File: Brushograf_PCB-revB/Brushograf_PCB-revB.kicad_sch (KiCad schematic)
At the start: 75 parts, among them J1 Conn_01x05_Socket, J12 USB-C PD in, J13 FluidDial pendant, J2 Conn_01x05_Socket, J3 Conn_01x05_Socket, J6 Conn_01x07_Socket, J7 Conn_01x03_Pin, J8 SD_CARD_MICRO_AMPHENOL_114008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, SW1 ESP POWER, U1 ULN2003A, U2 ULN2003A, U3 ULN2003A, U4 ESP32-DevKitC, U6 CH224K, U7 TPS54202, U8 TPS54202

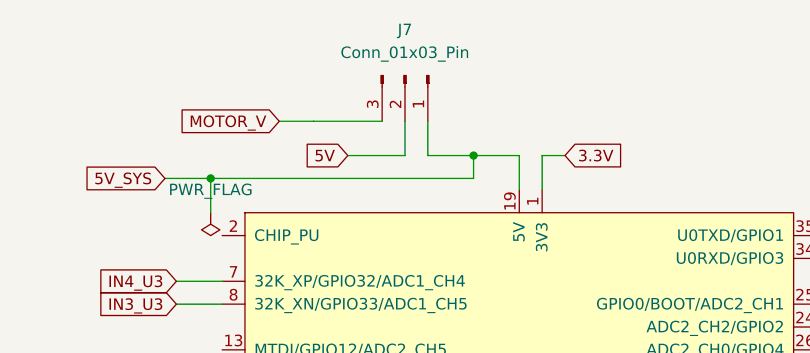
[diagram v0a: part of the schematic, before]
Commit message: Update SW2 to switch, move SW1 for hole clearance, relocate SD card holder to edge
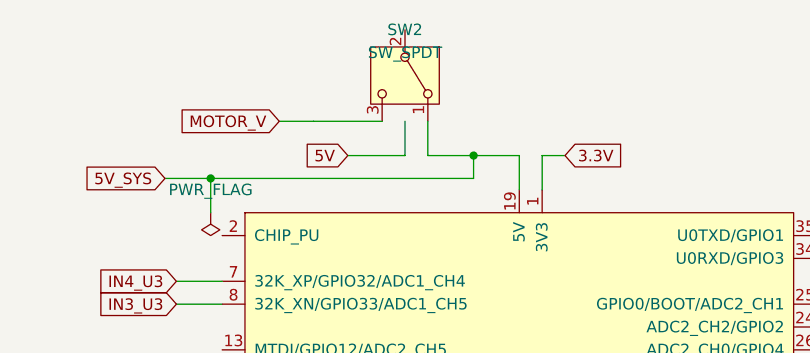
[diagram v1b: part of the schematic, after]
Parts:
- SW2: renamed from J7; value Conn_01x03_Pin -> SW_SPDT; footprint Connector_Molex:Molex_KK-254_AE-6410-03A_1x03_P2.54mm_Vertical -> Button_Switch_THT:SW_Slide_1P2T_EG1218; symbol Connector:Conn_01x03_Pin -> Switch:SW_SPDT
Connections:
- net 5V: no longer SW2.2 (Pin_2)
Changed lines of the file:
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@@
 	)
 	(symbol
-		(lib_id "Connector:Conn_01x03_Pin")
+		(lib_id "Switch:SW_SPDT")
 		(at 177.8 19.05 270)
 		(unit 1)
@@
 		(dnp no)
 		(fields_autoplaced yes)
-		(property "Reference" "J7"
+		(property "Reference" "SW2"
 			(at 177.8 13.97 90)
 			(effects
@@
 			)
 		)
-		(property "Value" "Conn_01x03_Pin"
+		(property "Value" "SW_SPDT"
 			(at 177.8 16.51 90)
 			(effects
@@
 			)
 		)
-		(property "Footprint" "Connector_Molex:Molex_KK-254_AE-6410-03A_1x03_P2.54mm_Vertical"
+		(property "Footprint" "Button_Switch_THT:SW_Slide_1P2T_EG1218"
 			(at 177.8 19.05 0)
 			(effects
@@
 			)
 		)
-		(property "Description" "Generic connector, single row, 01x03, script generated"
+		(property "Description" "Switch, single pole double throw"
 			(at 177.8 19.05 0)
 			(effects
@@
 			(project ""
 				(path "/d273ac3f-ed4f-4680-93b1-84a7dc3121ff"
-					(reference "J7")
+					(reference "SW2")
 					(unit 1)
 				)

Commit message: Remove unused components R13, R14, and J6
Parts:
- removed J6: Conn_01x07_Socket, Connector_Molex:Molex_KK-254_AE-6410-07A_1x07_P2.54mm_Vertical, symbol Connector:Conn_01x07_Socket
- removed R13, R14: 0, 007_dusjagr:R_1206_noGND, symbol Device:R
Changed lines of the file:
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@@
-	)
-	(symbol
-		(lib_id "Device:R")
-		(at 218.44 116.84 90)
-		(unit 1)
-		(exclude_from_sim no)
-		(in_bom yes)
-		(on_board yes)
-		(dnp no)
-		(fields_autoplaced yes)
-		(property "Reference" "R13"
-			(at 218.44 110.49 90)
-			(effects
-				(font
-					(size 1.27 1.27)
-				)
-			)
-		)
-		(property "Value" "0"
-			(at 218.44 113.03 90)
-			(effects
-				(font
-					(size 1.27 1.27)
-				)
-			)
-		)
-		(property "Footprint" "007_dusjagr:R_1206_noGND"
-			(at 218.44 118.618 90)
-			(effects
-				(font
-					(size 1.27 1.27)
-				)
-				(hide yes)
-			)
-		)
-		(property "Datasheet" "~"
-			(at 218.44 116.84 0)
-			(effects
-				(font
-					(size 1.27 1.27)
-				)
-				(hide yes)
-			)
-		)
-		(property "Description" "Resistor"
-			(at 218.44 116.84 0)
-			(effects
-				(font
-					(size 1.27 1.27)
-				)
-				(hide yes)
-			)
-		)
-		(pin "1"
-		)
-		(pin "2"
-		)
-		(instances
-			(project "Brusograf_PCB"
-				(path "/d273ac3f-ed4f-4680-93b1-84a7dc3121ff"
-					(reference "R13")
-					(unit 1)
-				)
-			)
-		)
 	)
 	(symbol
@@
 	)
 	(symbol
-		(lib_id "Device:R")
-		(at 209.55 116.84 90)
-		(unit 1)
-		(exclude_from_sim no)
-		(in_bom yes)
-		(on_board yes)
-		(dnp no)
-		(fields_autoplaced yes)
-		(property "Reference" "R14"
-			(at 209.55 110.49 90)
-			(effects
-				(font
-					(size 1.27 1.27)
-				)
-			)
-		)
-		(property "Value" "0"
-			(at 209.55 113.03 90)
-			(effects
-				(font
-					(size 1.27 1.27)
-				)
-			)
-		)
-		(property "Footprint" "007_dusjagr:R_1206_noGND"
-			(at 209.55 118.618 90)
-			(effects
-				(font
-					(size 1.27 1.27)
-				)
-				(hide yes)
-			)
-		)
-		(property "Datasheet" "~"
-			(at 209.55 116.84 0)
-			(effects
-				(font
-					(size 1.27 1.27)
-				)
-				(hide yes)
-			)
-		)
-		(property "Description" "Resistor"
-			(at 209.55 116.84 0)
-			(effects
-				(font
-					(size 1.27 1.27)
-				)
-				(hide yes)
-			)
-		)
-		(pin "1"
-		)
-		(pin "2"
-		)
-		(instances
-			(project "Brusograf_PCB"
-				(path "/d273ac3f-ed4f-4680-93b1-84a7dc3121ff"
-					(reference "R14")
-					(unit 1)
-				)
-			)
-		)
-	)
-	(symbol
 		(lib_id "power:GND")
 		(at 96.52 45.72 0)
@@
 					(unit 1)
 				)
-			)
-		)
-	)
-	(symbol
-		(lib_id "Connector:Conn_01x07_Socket")
-		(at 264.16 139.7 0)
-		(unit 1)
-		(exclude_from_sim no)
-		(in_bom yes)
-		(on_board yes)
-		(dnp no)
-		(fields_autoplaced yes)
-		(property "Reference" "J6"
-			(at 265.43 138.4299 0)
-			(effects
-				(font
-					(size 1.27 1.27)
-				)
-				(justify left)
-			)
-		)
-		(property "Value" "Conn_01x07_Socket"
-			(at 265.43 140.9699 0)
-			(effects
-				(font
-					(size 1.27 1.27)
-				)
-				(justify left)
-			)
-		)
-		(property "Footprint" "Connector_Molex:Molex_KK-254_AE-6410-07A_1x07_P2.54mm_Vertical"
-			(at 264.16 139.7 0)
-			(effects
-				(font
-					(size 1.27 1.27)
-				)
-				(hide yes)
-			)
-		)
-		(property "Datasheet" "~"
-			(at 264.16 139.7 0)
-			(effects
-				(font
-					(size 1.27 1.27)
-				)
-				(hide yes)
-			)
-		)
-		(property "Description" "Generic connector, single row, 01x07, script generated"
-			(at 264.16 139.7 0)
-			(effects
-				(font
-					(size 1.27 1.27)
-				)
-				(hide yes)
-			)
-		)
-		(pin "4"
-		)
-		(pin "3"
-		)
-		(pin "2"
-		)
-		(pin "1"
-		)
-		(pin "5"
-		)
-		(pin "6"
-		)
-		(pin "7"
-		)
-		(instances
-			(project ""
-				(path "/d273ac3f-ed4f-4680-93b1-84a7dc3121ff"
-					(reference "J6")
-					(unit 1)
-				)

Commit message: Add probe connector J7 and labels
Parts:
- added J7: Conn_01x03_Pin, Connector_PinHeader_2.54mm:PinHeader_1x03_P2.54mm_Vertical, symbol Connector:Conn_01x03_Pin
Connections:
- net 3.3V: now also J7.1 (Pin_1)
- net GND: now also J7.3 (Pin_3)
- net PROBE: now reaches U4.5 (VDET_1/GPIO34/ADC1_CH6)
- net PROBE: now also J7.2 (Pin_2)
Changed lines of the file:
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@@
 	)
 	(embedded_fonts no)
+	(symbol
+		(lib_id "Connector:Conn_01x03_Pin")
+		(at 260 140 0)
+		(unit 1)
+		(exclude_from_sim no)
+		(in_bom yes)
+		(on_board yes)
+		(dnp no)
+		(fields_autoplaced yes)
+		(property "Reference" "J7"
+			(at 260 132.38 0)
+			(effects
+				(font
+					(size 1.27 1.27)
+				)
+			)
+		)
+		(property "Value" "Conn_01x03_Pin"
+			(at 260 134.92 0)
+			(effects
+				(font
+					(size 1.27 1.27)
+				)
+			)
+		)
+		(property "Footprint" "Connector_PinHeader_2.54mm:PinHeader_1x03_P2.54mm_Vertical"
+			(at 260 140 0)
+			(effects
+				(font
+					(size 1.27 1.27)
+				)
+				(hide yes)
+			)
+		)
+		(property "Datasheet" "~"
+			(at 260 140 0)
+			(effects
+				(font
+					(size 1.27 1.27)
+				)
+				(hide yes)
+			)
+		)
+		(property "Description" "Generic connector, single row, 01x03, script generated"
+			(at 260 140 0)
+			(effects
+				(font
+					(size 1.27 1.27)
+				)
+				(hide yes)
+			)
+		)
+		(pin "1"
+		)
+		(pin "2"
+		)
+		(pin "3"
+		)
+		(instances
+			(project "Brusograf_PCB"
+				(path "/d273ac3f-ed4f-4680-93b1-84a7dc3121ff"
+					(reference "J7")
+					(unit 1)
+				)
+			)
+		)
+	)
+	(global_label "3.3V"
+		(shape input)
+		(at 265.08 137.46 0)
+		(fields_autoplaced yes)
+		(effects
+			(font
+				(size 1.27 1.27)
+			)
+			(justify left)
+		)
+		(property "Intersheetrefs" "${INTERSHEET_REFS}"
+			(at 270 137.46 0)
+			(effects
+				(font
+					(size 1.27 1.27)
+				)
+				(hide yes)
+			)
+		)
+	)
+	(global_label "PROBE"
+		(shape input)
+		(at 265.08 140 0)
+		(fields_autoplaced yes)
+		(effects
+			(font
+				(size 1.27 1.27)
+			)
+			(justify left)
+		)
+		(property "Intersheetrefs" "${INTERSHEET_REFS}"
+			(at 270 140 0)
+			(effects
+				(font
+					(size 1.27 1.27)
+				)
+				(hide yes)
+			)
+		)
+	)
+	(global_label "GND"
+		(shape input)
+		(at 265.08 142.54 0)
+		(fields_autoplaced yes)
+		(effects
+			(font
+				(size 1.27 1.27)
+			)
+			(justify left)
+		)
+		(property "Intersheetrefs" "${INTERSHEET_REFS}"
+			(at 270 142.54 0)
+			(effects
+				(font
+					(size 1.27 1.27)
+				)
+				(hide yes)
+			)
+		)
+	)
+	(global_label "PROBE"
+		(shape input)
+		(at 157.48 62.23 180)
+		(fields_autoplaced yes)
+		(effects
+			(font
+				(size 1.27 1.27)
+			)
+			(justify right)
+		)
+		(property "Intersheetrefs" "${INTERSHEET_REFS}"
+			(at 152 62.23 0)
+			(effects
+				(font
+					(size 1.27 1.27)
+				)
+				(hide yes)
+			)
+		)
+	)
 )

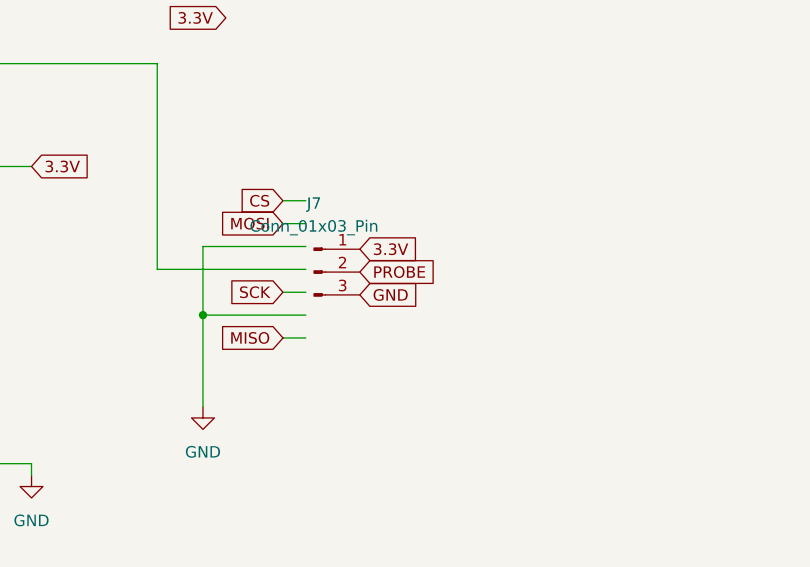
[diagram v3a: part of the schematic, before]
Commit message: Move J7 to Y=50 and swap GND/PROBE pinout
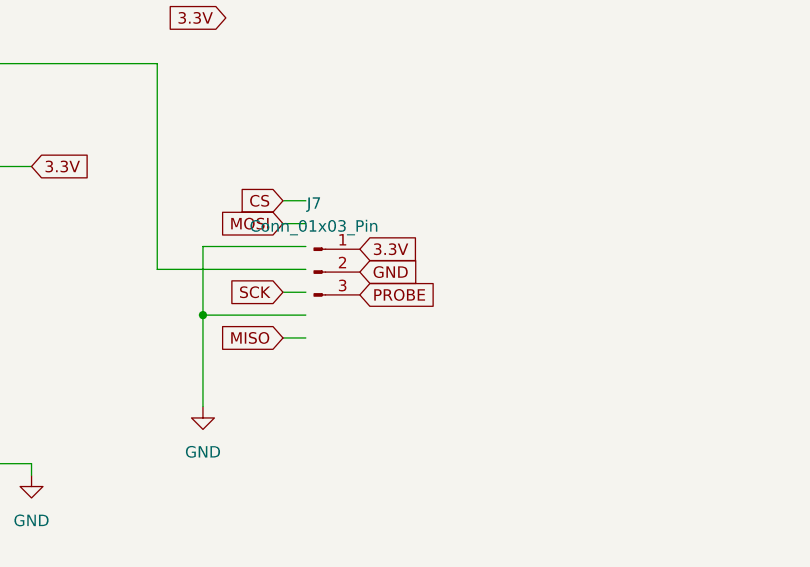
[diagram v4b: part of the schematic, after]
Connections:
- net GND: now also J7.2 (Pin_2); no longer J7.3 (Pin_3)
- net PROBE: now also J7.3 (Pin_3); no longer J7.2 (Pin_2)
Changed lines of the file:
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@@
 		(instances
 			(project "Brusograf_PCB"
-				(path "/d273ac3f-ed4f-4680-93b1-84a7dc3121ff"
+				(path "/d273ac3f-ed4f-4680-93b1-84a7dc3121ff/1b34f1d6-21dc-4342-b709-854909a60127"
 					(reference "J7")
 					(unit 1)
@@
 		)
 	)
-	(global_label "PROBE"
+	(global_label "GND"
 		(shape input)
 		(at 265.08 140 0)
@@
 		)
 	)
-	(global_label "GND"
+	(global_label "PROBE"
 		(shape input)
 		(at 265.08 142.54 0)

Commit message: Move USB-C to Y=15.84 and Switches to Y=22. Add LEDs with Brushograph footprints
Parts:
- added D_SW1, D_SW2, D_USB: LED, 009_Brushograph:LED_D1.8mm_Brushograf, symbol Device:LED
- added R_SW1, R_SW2, R_USB: 1k, 007_dusjagr:R_1206_noGND, symbol Device:R
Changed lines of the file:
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@@
 		)
 	)
+	(symbol
+		(lib_id "Device:LED")
+		(at 20 40 0)
+		(unit 1)
+		(exclude_from_sim no)
+		(in_bom yes)
+		(on_board yes)
+		(dnp no)
+		(fields_autoplaced yes)
+		(property "Reference" "D_USB" (at 20 30 0) (effects (font (size 1.27 1.27))))
+		(property "Value" "LED" (at 20 32 0) (effects (font (size 1.27 1.27))))
+		(property "Footprint" "009_Brushograph:LED_D1.8mm_Brushograf" (at 20 40 0) (effects (font (size 1.27 1.27)) (hide yes)))
+		(pin "1")
+		(pin "2")
+		(instances (project "Brusograf_PCB" (path "/d273ac3f-ed4f-4680-93b1-84a7dc3121ff" (reference "D_USB") (unit 1))))
+	)
+	(symbol
+		(lib_id "Device:R")
+		(at 20 45 0)
+		(unit 1)
+		(exclude_from_sim no)
+		(in_bom yes)
+		(on_board yes)
+		(dnp no)
+		(fields_autoplaced yes)
+		(property "Reference" "R_USB" (at 20 50 0) (effects (font (size 1.27 1.27))))
+		(property "Value" "1k" (at 20 52 0) (effects (font (size 1.27 1.27))))
+		(property "Footprint" "007_dusjagr:R_1206_noGND" (at 20 45 0) (effects (font (size 1.27 1.27)) (hide yes)))
+		(pin "1")
+		(pin "2")
+		(instances (project "Brusograf_PCB" (path "/d273ac3f-ed4f-4680-93b1-84a7dc3121ff" (reference "R_USB") (unit 1))))
+	)
+	(symbol
+		(lib_id "Device:LED")
+		(at 30 40 0)
+		(unit 1)
+		(exclude_from_sim no)
+		(in_bom yes)
+		(on_board yes)
+		(dnp no)
+		(fields_autoplaced yes)
+		(property "Reference" "D_SW1" (at 30 30 0) (effects (font (size 1.27 1.27))))
+		(property "Value" "LED" (at 30 32 0) (effects (font (size 1.27 1.27))))
+		(property "Footprint" "009_Brushograph:LED_D1.8mm_Brushograf" (at 30 40 0) (effects (font (size 1.27 1.27)) (hide yes)))
+		(pin "1")
+		(pin "2")
+		(instances (project "Brusograf_PCB" (path "/d273ac3f-ed4f-4680-93b1-84a7dc3121ff" (reference "D_SW1") (unit 1))))
+	)
+	(symbol
+		(lib_id "Device:R")
+		(at 30 45 0)
+		(unit 1)
+		(exclude_from_sim no)
+		(in_bom yes)
+		(on_board yes)
+		(dnp no)
+		(fields_autoplaced yes)
+		(property "Reference" "R_SW1" (at 30 50 0) (effects (font (size 1.27 1.27))))
+		(property "Value" "1k" (at 30 52 0) (effects (font (size 1.27 1.27))))
+		(property "Footprint" "007_dusjagr:R_1206_noGND" (at 30 45 0) (effects (font (size 1.27 1.27)) (hide yes)))
+		(pin "1")
+		(pin "2")
+		(instances (project "Brusograf_PCB" (path "/d273ac3f-ed4f-4680-93b1-84a7dc3121ff" (reference "R_SW1") (unit 1))))
+	)
+	(symbol
+		(lib_id "Device:LED")
+		(at 40 40 0)
+		(unit 1)
+		(exclude_from_sim no)
+		(in_bom yes)
+		(on_board yes)
+		(dnp no)
+		(fields_autoplaced yes)
+		(property "Reference" "D_SW2" (at 40 30 0) (effects (font (size 1.27 1.27))))
+		(property "Value" "LED" (at 40 32 0) (effects (font (size 1.27 1.27))))
+		(property "Footprint" "009_Brushograph:LED_D1.8mm_Brushograf" (at 40 40 0) (effects (font (size 1.27 1.27)) (hide yes)))
+		(pin "1")
+		(pin "2")
+		(instances (project "Brusograf_PCB" (path "/d273ac3f-ed4f-4680-93b1-84a7dc3121ff" (reference "D_SW2") (unit 1))))
+	)
+	(symbol
+		(lib_id "Device:R")
+		(at 40 45 0)
+		(unit 1)
+		(exclude_from_sim no)
+		(in_bom yes)
+		(on_board yes)
+		(dnp no)
+		(fields_autoplaced yes)
+		(property "Reference" "R_SW2" (at 40 50 0) (effects (font (size 1.27 1.27))))
+		(property "Value" "1k" (at 40 52 0) (effects (font (size 1.27 1.27))))
+		(property "Footprint" "007_dusjagr:R_1206_noGND" (at 40 45 0) (effects (font (size 1.27 1.27)) (hide yes)))
+		(pin "1")
+		(pin "2")
+		(instances (project "Brusograf_PCB" (path "/d273ac3f-ed4f-4680-93b1-84a7dc3121ff" (reference "R_SW2") (unit 1))))
+	)
 )
